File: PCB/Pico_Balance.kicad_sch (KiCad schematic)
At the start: 33 parts, among them Q1 NMOS, U1 BMI160, U2 DRV8876PWPR, U3 DRV8876PWPR, U4 LM74610QDGKRQ1, U5 LMR51430

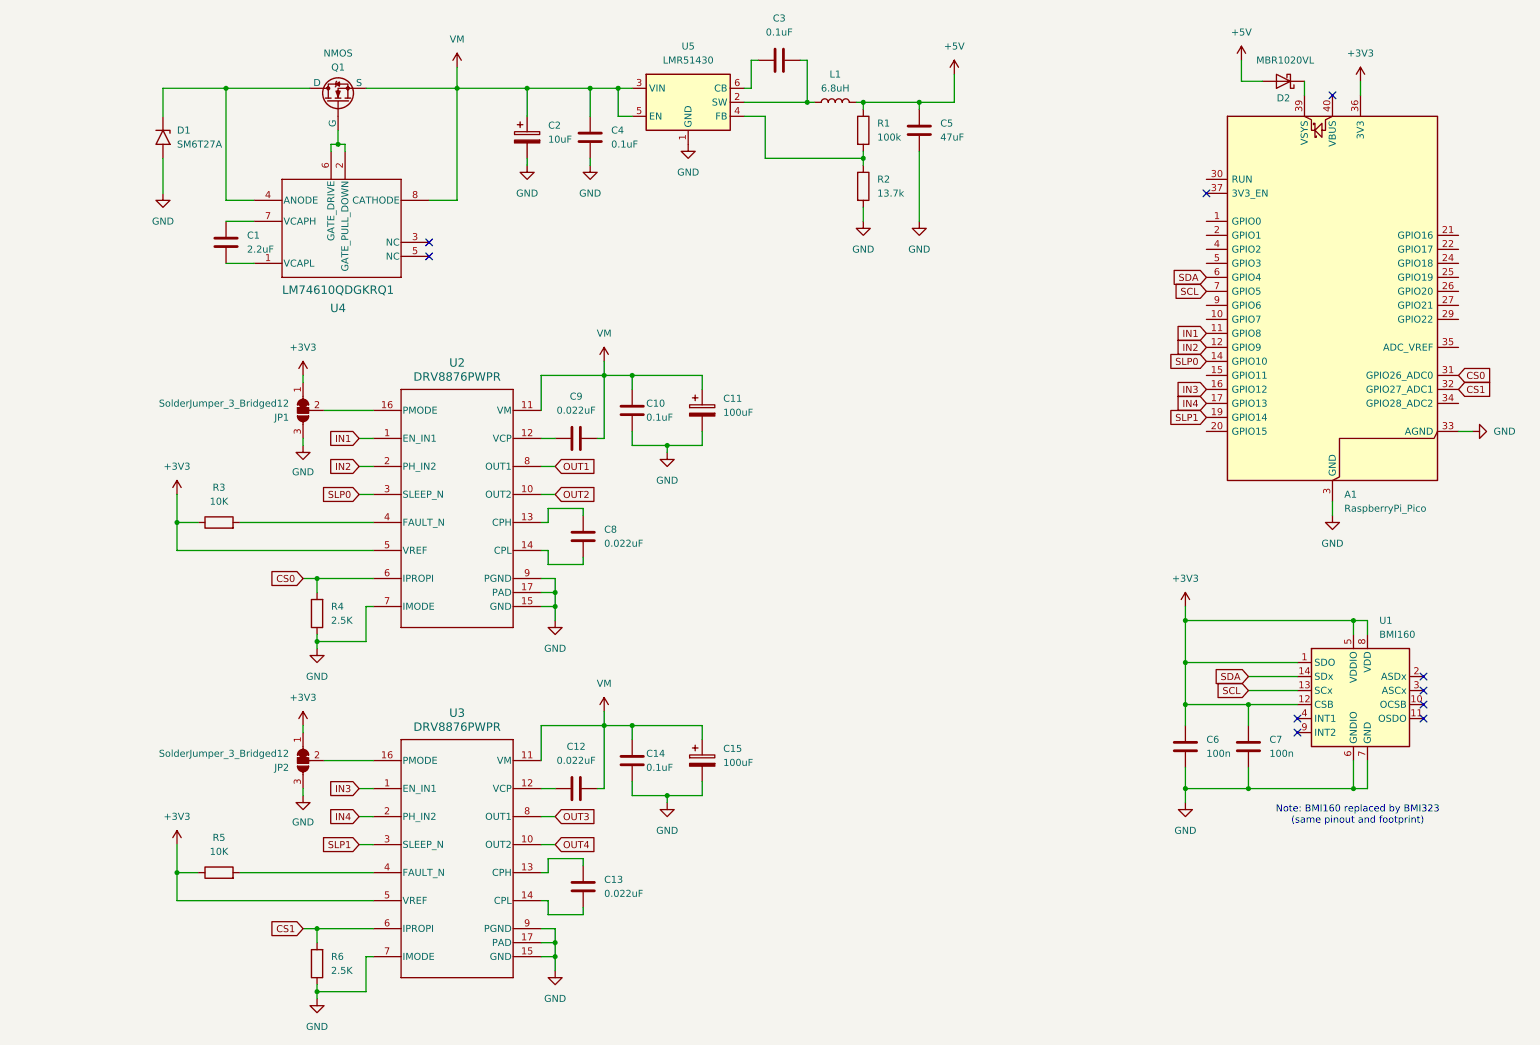
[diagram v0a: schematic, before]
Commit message: Schematic Refinement and some footprint assignment
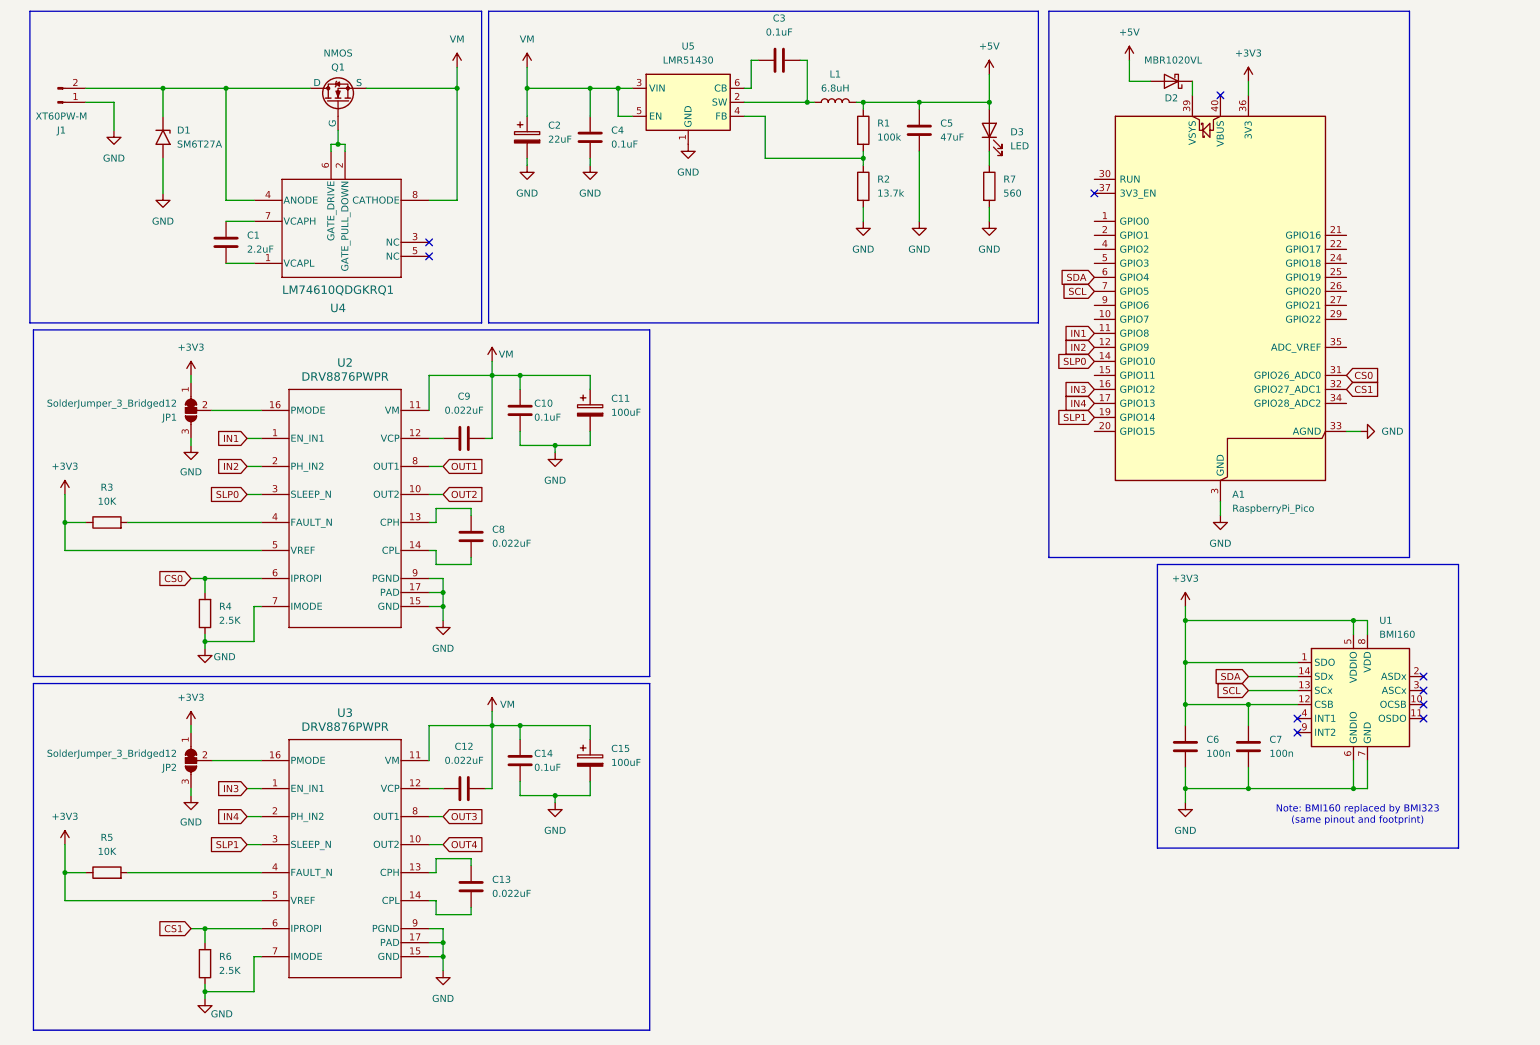
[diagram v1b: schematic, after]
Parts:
- added D3: LED, LED_SMD:LED_0805_2012Metric, symbol Device:LED
- added J1: XT60PW-M, Connector_AMASS:AMASS_XT60PW-M_1x02_P7.20mm_Horizontal, symbol Connector:Conn_01x02_Pin
- added R7: 560, symbol Device:R
- C2: value 10uF -> 22uF
- Q1: footprint (none) -> Package_SO:SO-8_3.9x4.9mm_P1.27mm
- U2, U3: footprint PWP0016J_N -> footprints:PWP0016J_N
- U4: footprint DGK0008A_N -> footprints:DGK0008A_N
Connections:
- net +5V: now also D3.2 (A)
- net GND: now also J1.1 (Pin_1), R7.2
- net at D1.1 (A1), Q1.1 (D), U4.4 (ANODE): now also J1.2 (Pin_2)
- new net: D3.1 (K), R7.1
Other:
- moved on the sheet: A1, C10, C11, C12, C13, C14, C15, C8, C9, D2, JP1, JP2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

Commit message: Footprint Assignment
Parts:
- added J2: GPIO_Ext, Connector_PinHeader_2.54mm:PinHeader_2x06_P2.54mm_Vertical, symbol Connector_Generic:Conn_02x06_Odd_Even
- added J3, J4: Conn_01x06_Pin, Connector_PinSocket_2.54mm:PinSocket_1x06_P2.54mm_Vertical, symbol Connector:Conn_01x06_Pin
- C1: footprint (none) -> Capacitor_SMD:C_1206_3216Metric
- C10, C12, C13, C14, C3, C4, C6, C7, C8, C9: footprint (none) -> Capacitor_SMD:C_0603_1608Metric
- C11, C15: footprint (none) -> Capacitor_SMD:CP_Elec_10x10.5
- C2: footprint (none) -> Capacitor_SMD:CP_Elec_5x5.4
- C5: footprint (none) -> Capacitor_SMD:C_1210_3225Metric
- L1: footprint (none) -> Inductor_SMD:L_APV_APH0630
- R1, R2, R3, R4, R5, R6, R7: footprint (none) -> Resistor_SMD:R_0603_1608Metric
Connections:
- net +3V3: now also J2.1 (Pin_1), J3.2 (Pin_2), J4.2 (Pin_2)
- net +5V: now also J2.2 (Pin_2), J2.4 (Pin_4)
- net GND: now also J2.6 (Pin_6), J2.8 (Pin_8), J3.5 (Pin_5), J4.5 (Pin_5)
- net OUT1: now also J3.6 (Pin_6), J4.6 (Pin_6)
- net OUT2: now also J3.1 (Pin_1), J4.1 (Pin_1)
- net SCL: now also J2.10 (Pin_10)
- net SDA: now also J2.12 (Pin_12)
- net SLP1: now also A1.15 (GPIO11); no longer A1.19 (GPIO14)
- net ENCB0: now reaches A1.10 (GPIO7)
- net ENCB0: now also J3.4 (Pin_4)
- net ENCB1: now reaches A1.20 (GPIO15)
- net ENCB1: now also J4.4 (Pin_4)
- net at A1.21 (GPIO16): now also J2.3 (Pin_3)
- net at A1.22 (GPIO17): now also J2.5 (Pin_5)
- net at A1.24 (GPIO18): now also J2.7 (Pin_7)
- net at A1.25 (GPIO19): now also J2.9 (Pin_9)
- net at A1.26 (GPIO20): now also J2.11 (Pin_11)
- net ENCA0: now reaches A1.9 (GPIO6)
- net ENCA0: now also J3.3 (Pin_3)
- new net ENCA1: A1.19 (GPIO14), J4.3 (Pin_3)
- no-connect marks 10 -> 18
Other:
- moved on the sheet: A1, D2

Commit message: Very Initial Layout and footprint updates
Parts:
- removed Q1: NMOS, Package_SO:SO-8_3.9x4.9mm_P1.27mm, symbol Simulation_SPICE:NMOS
- added Q1: CSD17577Q3A, Package_SON:VSON-8_3.3x3.3mm_P0.65mm_NexFET, symbol Transistor_FET:CSD17577Q3A
- C11, C15: value 100uF -> 330uF
- D1: value SM6T27A -> SM6T30A; footprint LED_SMD:LED-L1T2_LUMILEDS -> Diode_SMD:D_SMB
- J3: value Conn_01x06_Pin -> Conn_Motor0
- J4: value Conn_01x06_Pin -> Conn_Motor1
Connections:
- net OUT1: no longer J4.6 (Pin_6)
- net OUT2: no longer J4.1 (Pin_1)
- net OUT3: now also J4.6 (Pin_6)
- net OUT4: now also J4.1 (Pin_1)
- net VM: now also Q1.1 (S), Q1.2 (S), Q1.3 (S)
- net at D1.1 (A1), J1.2 (Pin_2), U4.4 (ANODE): now also Q1.5 (D)
- net at U4.2 (GATE_PULL_DOWN), U4.6 (GATE_DRIVE): now also Q1.4 (G)
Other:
- note added: "5V Regulation"
- note added: "Battery Input Protection"
- note added: "IMU"
- note added: "Motor Driver 0"
- note added: "Motor Driver 1"
- note added: "Pi Pico MCU"
- moved on the sheet: J3, J4

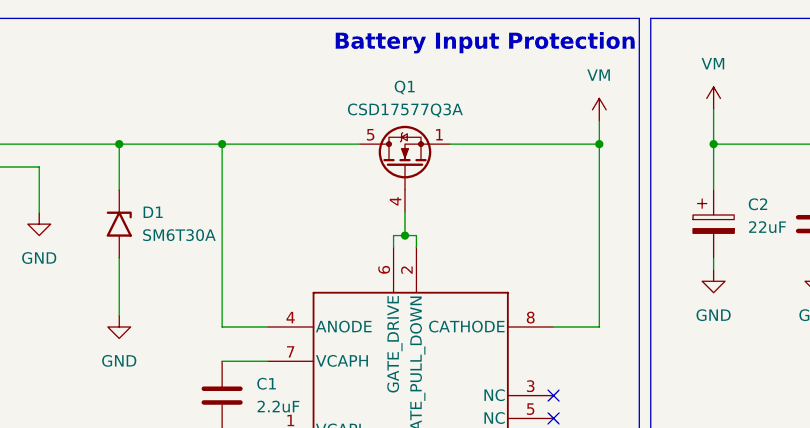
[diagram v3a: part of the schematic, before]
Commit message: Initial Input Protection Layout
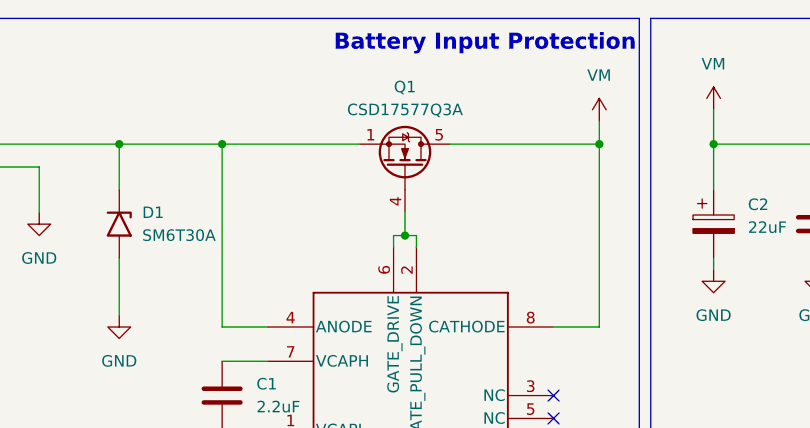
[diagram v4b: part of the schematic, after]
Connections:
- net VM: now also Q1.5 (D); no longer Q1.1 (S), Q1.2 (S), Q1.3 (S)
- net at D1.1 (A1), J1.2 (Pin_2), U4.4 (ANODE): now also Q1.1 (S), Q1.2 (S), Q1.3 (S); no longer Q1.5 (D)
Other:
- moved on the sheet: Q1
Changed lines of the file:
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@@
 	(symbol
 		(lib_id "Transistor_FET:CSD17577Q3A")
-		(at 68.58 29.21 90)
+		(at 68.58 29.21 270)
+		(mirror x)
 		(unit 1)
 		(exclude_from_sim no)
@@
 		(on_board yes)
 		(dnp no)
-		(fields_autoplaced yes)
 		(property "Reference" "Q1"
 			(at 68.58 20.32 90)
@@
 		)
 		(property "Footprint" "Package_SON:VSON-8_3.3x3.3mm_P0.65mm_NexFET"
-			(at 70.485 24.13 0)
+			(at 66.675 24.13 0)
 			(effects
 				(font
@@
 		)
 		(property "Datasheet" "https://www.ti.com/lit/ds/symlink/csd17577q3a.pdf"
-			(at 72.39 24.13 0)
+			(at 64.77 24.13 0)
 			(effects
 				(font

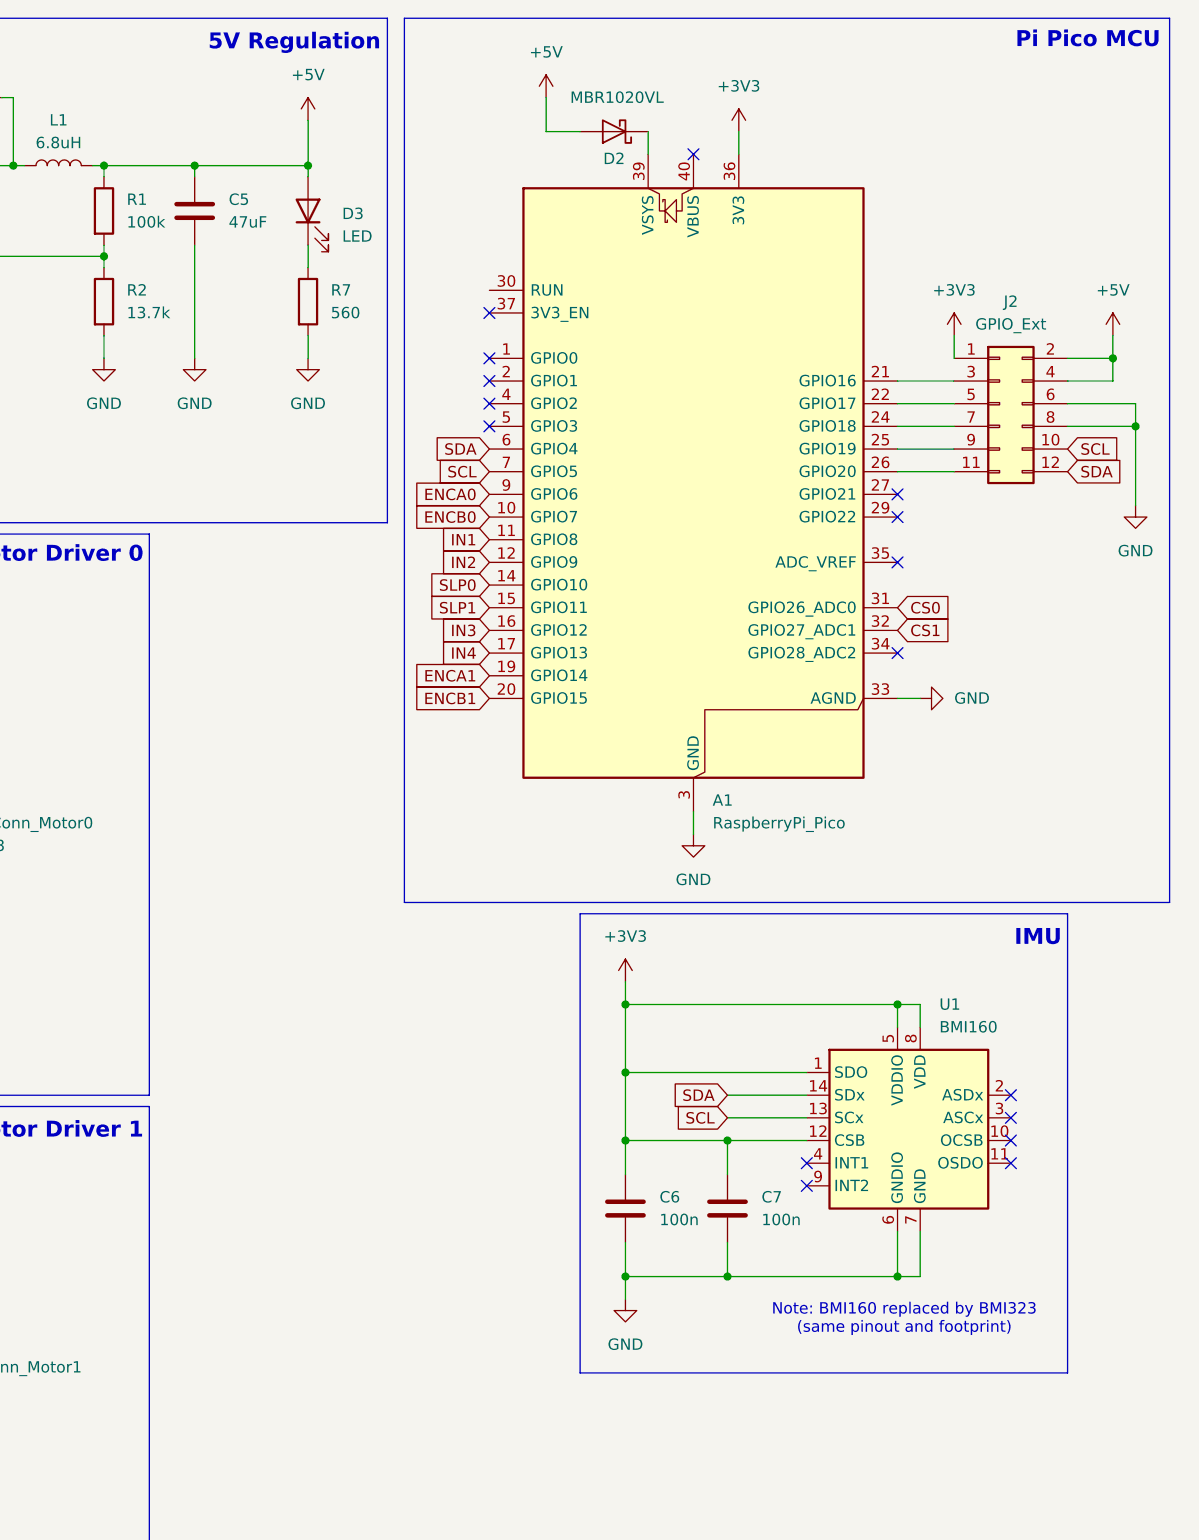
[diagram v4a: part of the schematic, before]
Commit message: Layout Refinements and add USB C port for power
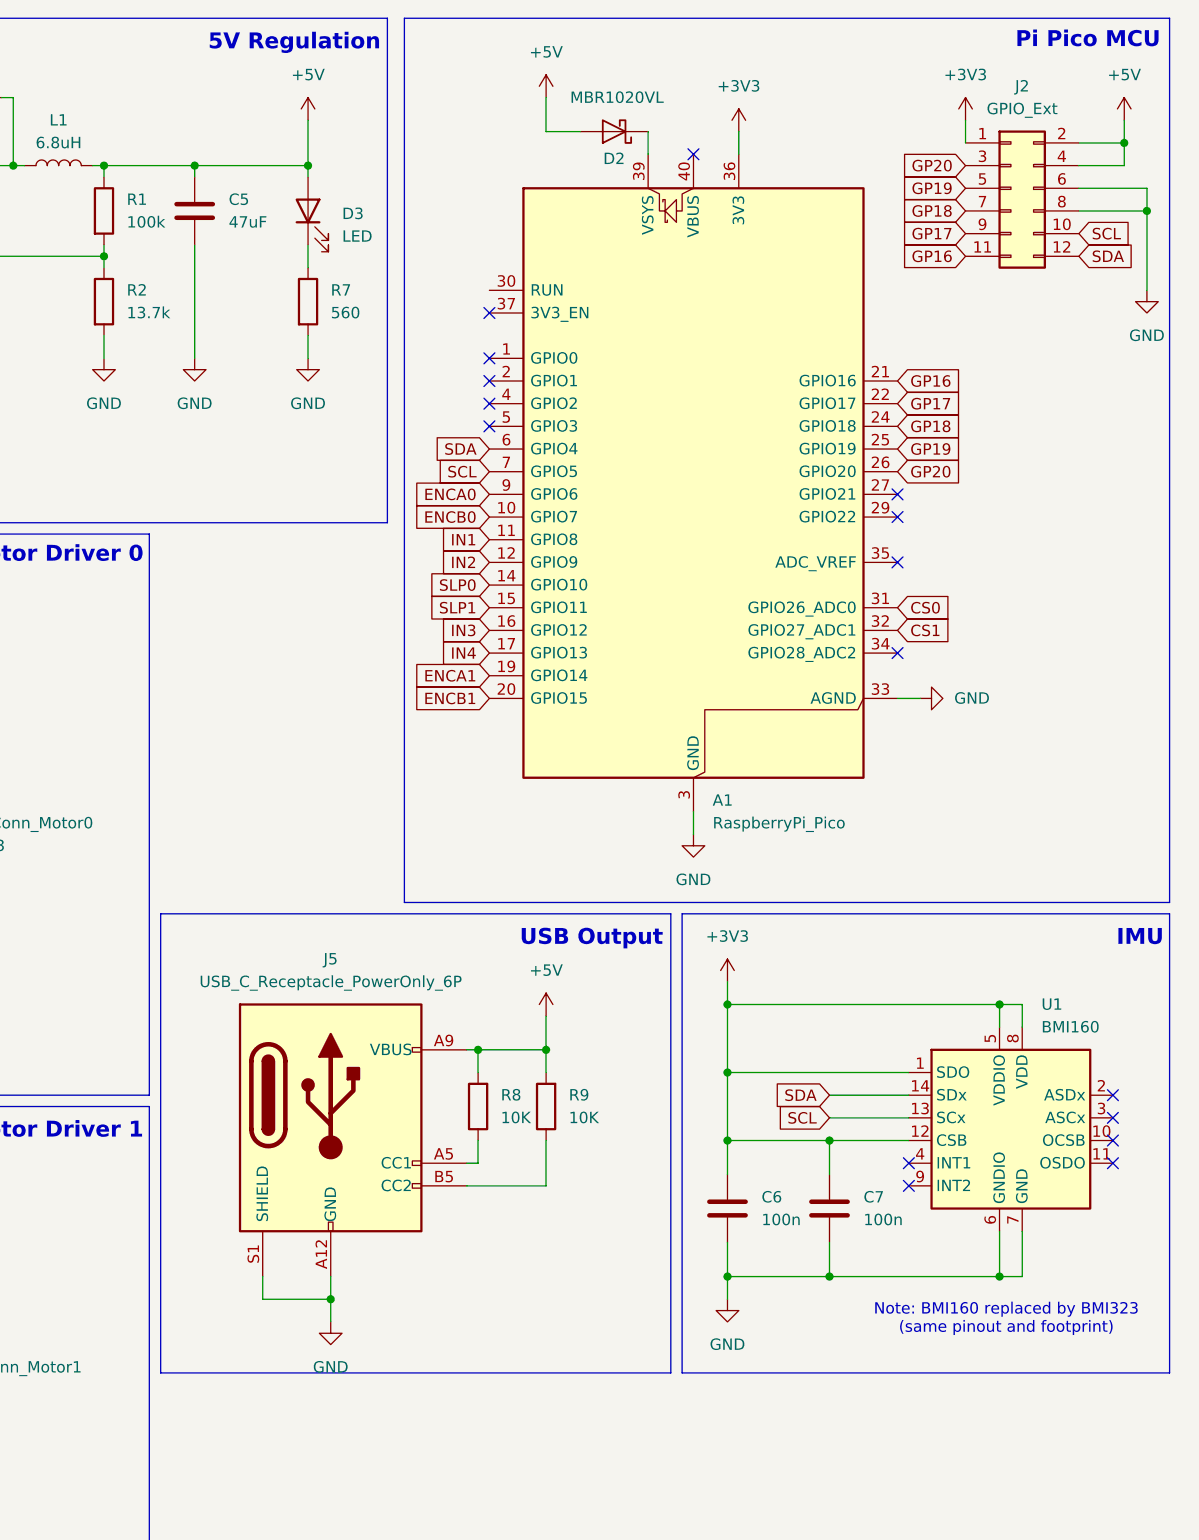
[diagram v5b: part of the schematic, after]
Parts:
- added J5: USB_C_Receptacle_PowerOnly_6P, Connector_USB:USB_C_Receptacle_HRO_TYPE-C-31-M-17, symbol Connector:USB_C_Receptacle_PowerOnly_6P
- added R8, R9: 10K, Resistor_SMD:R_0603_1608Metric, symbol Device:R
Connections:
- net +5V: now also J5.A9 (VBUS), J5.B9 (VBUS), R8.2, R9.2
- net GND: now also J5.A12 (GND), J5.B12 (GND), J5.S1 (SHIELD)
- net GP16: now reaches J2.11 (Pin_11)
- net GP16: now also A1.21 (GPIO16); no longer A1.26 (GPIO20)
- net GP20: now reaches J2.3 (Pin_3)
- net GP20: now also A1.26 (GPIO20); no longer A1.21 (GPIO16)
- net GP17: now reaches A1.22 (GPIO17)
- net GP17: now also J2.9 (Pin_9); no longer J2.5 (Pin_5)
- net GP18: now reaches A1.24 (GPIO18), J2.7 (Pin_7)
- net GP19: now reaches A1.25 (GPIO19)
- net GP19: now also J2.5 (Pin_5); no longer J2.9 (Pin_9)
- new net: J5.A5 (CC1), R8.1
- new net: J5.B5 (CC2), R9.1
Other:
- note added: "USB Output"
- moved on the sheet: C6, C7, J2, U1
